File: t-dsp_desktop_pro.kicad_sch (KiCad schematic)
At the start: 177 parts, among them IC1 Logic Level Shifter - 74HCT2G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, J1 jumper, J10 JST-XH Connector -, J11 JST-XH Connector -, J12 RGB LED HEADEER, J13 Conn_01x02, J14 Conn_01x03, J15 Conn_01x01, J16 Conn_01x02, J17 Conn_02x04_Odd_Even, J18 Conn_02x02_Odd_Even, J2 GROUND HEADER, J3 jumper, J4 jumper, J5 jumper, J6 jumper, J7 jumper, J8 PJRAS2X1S01X, J9 PJRAS2X1S01X, SW1 SW_SPST, SW2 TL1105WF160Q - 3.15mm actuator, SW3 SW_SPST, SW4 SW_SPST, SW5 RotaryEncoder_Switch_MP, SW6 TL1105WF160Q - 3.15mm actuator, SW7 TL1105WF160Q - 3.15mm actuator, SW8 TL1105WF160Q - 3.15mm actuator, T108 Tab, T109 Tab, T110 Tab, T111 Tab, U1 Teensy 4.1 - DEVKIT, U2 ESP32-DevKitC - DEVKIT, U3 Power Mux & Protect - TPS2116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, U4 Optoisolators - H11L1SM - 6-S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, U5 Dual Buffer - SN74LVC2G125DCTR, U6 Dual Buffer - SN74LVC2G125DCTR, U7 Dual Buffer - SN74LVC2G125DCTR, U8 Dual Buffer - SN74LVC2G125DCTR, U9 Dual Buffer - 74HCT2G17GW,125

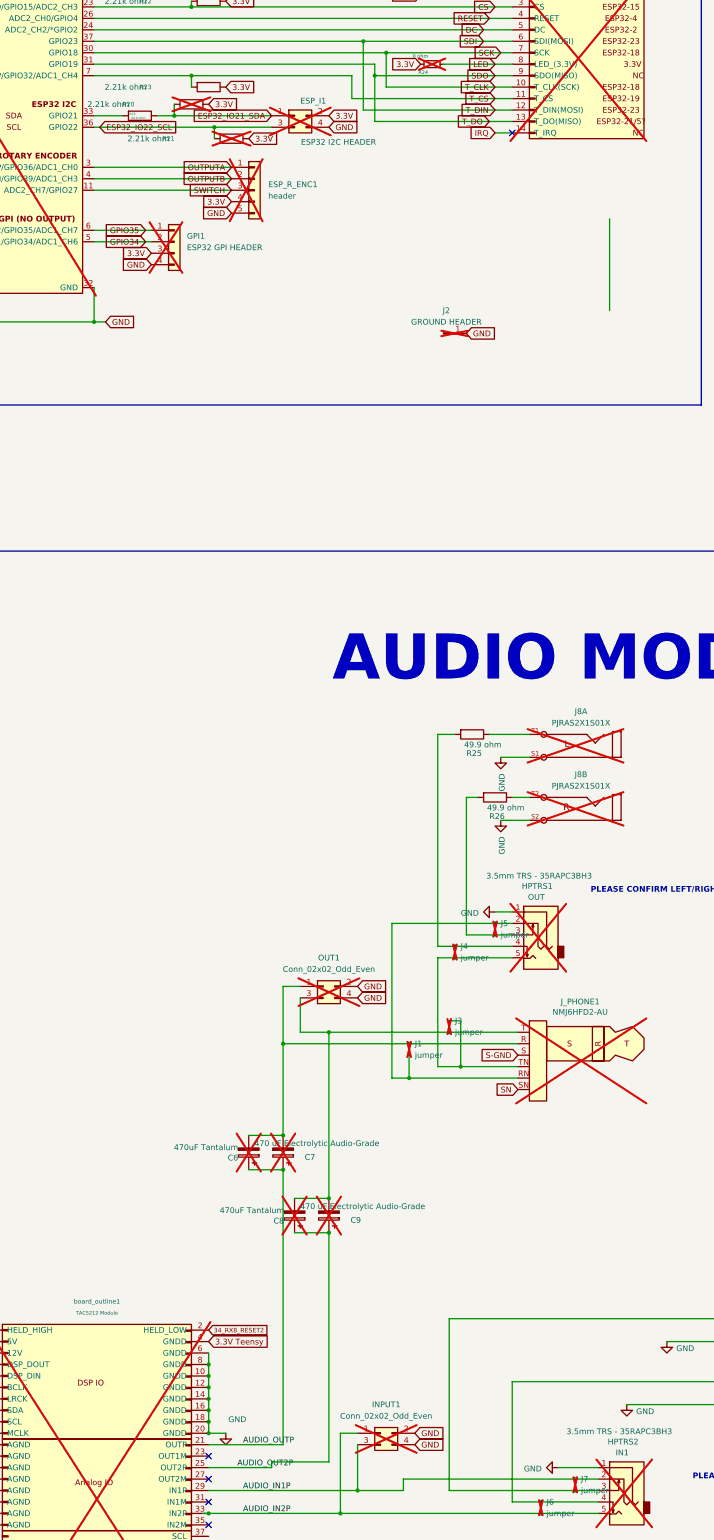
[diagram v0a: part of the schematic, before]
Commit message: Localize all 3D model paths for Docker/CI rendering
Rewrite all 3D model references from system variables (KICAD9_3DMODEL_DIR,
KISYS3DMOD, KICAD6/8_3DMODEL_DIR) to ${KIPRJMOD}/3d_models/ so models
resolve correctly in Docker-based KiBot CI builds. Copy 45 standard KiCad
3D models to the project. Fix BOM field mismatches for RLED1/RLED2 and
R36/R39 grouping. Update schematic symbol library and footprint libraries.

Co-Authored-By: Claude Opus 4.6 <noreply@anthropic.com>
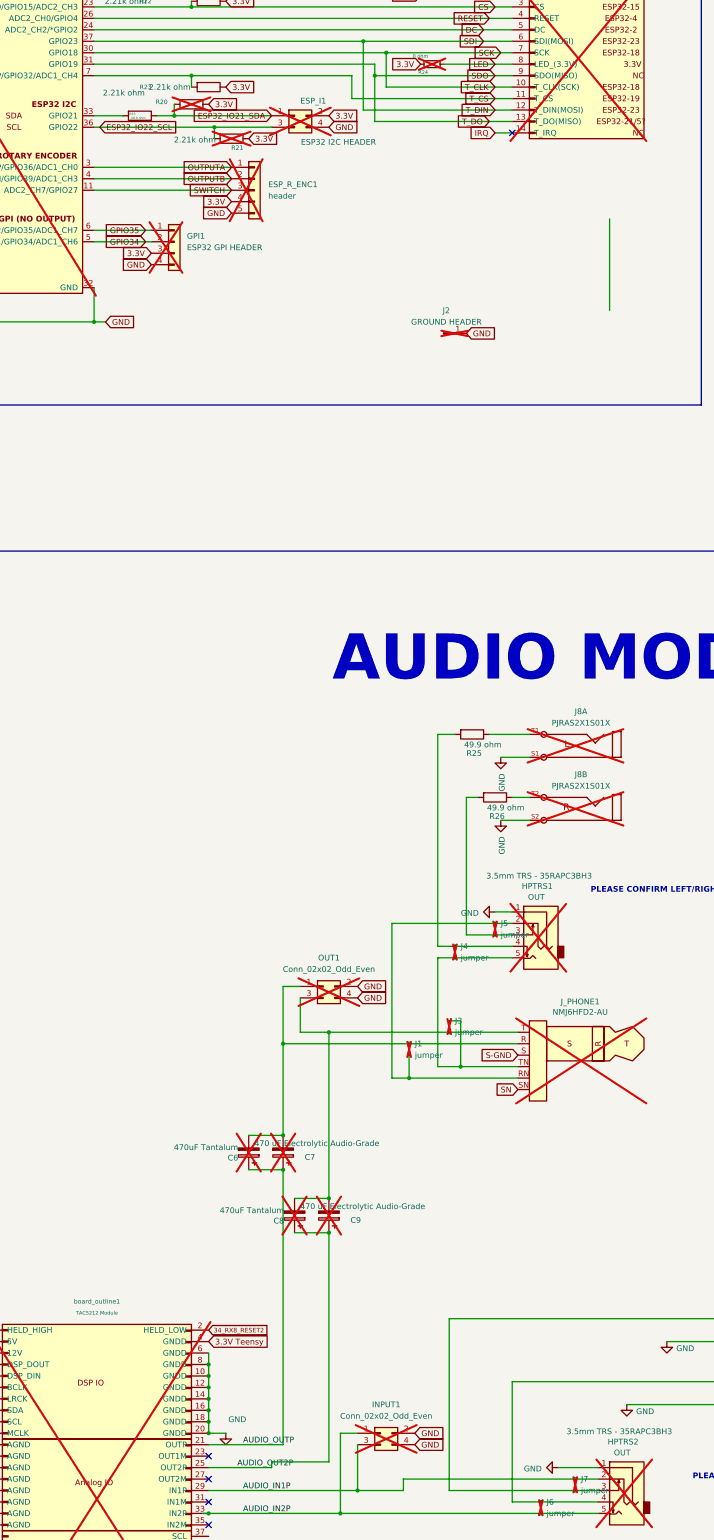
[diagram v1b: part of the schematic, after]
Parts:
- HPTRS1: symbol 35RAPC3BH3:AudioJack3_SwitchTR -> project_sch:HPTRS1
- HPTRS2: symbol 35RAPC3BH3:AudioJack3_SwitchTR -> project_sch:HPTRS1; Label IN1 -> OUT
- R20, R21: now in the parts list
- R36, R39: Manufacturer YAGEO -> Bourns; Manufacturer_Part_Number RC0805JR-0747RL -> CR0805-FX-2200ELF
- RLED1, RLED2: Digikey P100BYCT-ND -> ERJ-PA2F2211X-ND; Manufacturer Bourns -> YAGEO; Manufacturer_Part_Number CMP0805AFX-1000ELF -> RC0805DR-072K2L
- board_outline1: footprint project_fp:audio_module_board_outline_50x34.5_d1_mod -> project_fp:audio_module_board_outline_50x34.5_d1
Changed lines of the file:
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@@
 	)
 	(symbol
-		(lib_name "AudioJack3_SwitchTR_1")
-		(lib_id "35RAPC3BH3:AudioJack3_SwitchTR")
+		(lib_id "project_sch:HPTRS1")
 		(at 533.4 695.96 0)
 		(mirror y)
@@
 			)
 		)
-		(property "Label" "IN1"
+		(property "Label" "OUT"
 			(at 533.654 690.118 0)
 			(effects
@@
 		(unit 1)
 		(exclude_from_sim no)
-		(in_bom no)
+		(in_bom yes)
 		(on_board yes)
 		(dnp yes)
 		(property "Reference" "R21"
-			(at 433.07 398.78 90)
+			(at 448.31 400.812 90)
 			(effects
 				(font
@@
 		)
 		(property "Value" "2.21k ohm"
-			(at 428.625 398.78 90)
+			(at 438.912 399.034 90)
 			(effects
 				(font
@@
 		(unit 1)
 		(exclude_from_sim no)
-		(in_bom no)
+		(in_bom yes)
 		(on_board yes)
 		(dnp yes)
 		(property "Reference" "R20"
-			(at 424.18 391.16 90)
+			(at 431.546 390.652 90)
 			(effects
 				(font
@@
 		)
 		(property "Value" "2.21k ohm"
-			(at 419.735 391.16 90)
+			(at 433.324 387.35 90)
 			(effects
 				(font
@@
 			)
 		)
-		(property "Footprint" "project_fp:audio_module_board_outline_50x34.5_d1_mod"
+		(property "Footprint" "project_fp:audio_module_board_outline_50x34.5_d1"
 			(at 416.56 703.58 0)
 			(effects
@@
 			)
 		)
-		(property "Description" ""
+		(property "Description" "RES SMD 2.21 KOHM 1% 1/5W 0402"
 			(at 760.73 312.42 0)
 			(effects
@@
 					(size 1.27 1.27)
 				)
+				(hide yes)
 			)
 		)
-		(property "Manufacturer_Part_Number" "CMP0805AFX-1000ELF"
+		(property "Manufacturer_Part_Number" "RC0805DR-072K2L"
 			(at 760.73 312.42 0)
 			(effects
@@
 			)
 		)
-		(property "Digikey" "P100BYCT-ND"
+		(property "Digikey" "ERJ-PA2F2211X-ND"
 			(at 760.73 312.42 0)
 			(effects
@@
 			)
 		)
-		(property "Manufacturer" "Bourns"
+		(property "Manufacturer" "YAGEO"
 			(at 760.73 312.42 0)
 			(effects
@@
 			)
 		)
-		(property "Description" ""
+		(property "Description" "RES SMD 2.21 KOHM 1% 1/5W 0402"
 			(at 760.73 297.18 0)
 			(effects
@@
 					(size 1.27 1.27)
 				)
+				(hide yes)
 			)
 		)
-		(property "Manufacturer_Part_Number" "CMP0805AFX-1000ELF"
+		(property "Manufacturer_Part_Number" "RC0805DR-072K2L"
 			(at 760.73 297.18 0)
 			(effects
@@
 			)
 		)
-		(property "Digikey" "P100BYCT-ND"
+		(property "Digikey" "ERJ-PA2F2211X-ND"
 			(at 760.73 297.18 0)
 			(effects
@@
 			)
 		)
-		(property "Manufacturer" "Bourns"
+		(property "Manufacturer" "YAGEO"
 			(at 760.73 297.18 0)
 			(effects
@@
 		)
 		(property "Value" "2.21k ohm"
-			(at 423.545 387.35 90)
+			(at 423.164 388.62 90)
 			(effects
 				(font
@@
 			)
 		)
-		(property "Manufacturer" "YAGEO"
+		(property "Manufacturer" "Bourns"
 			(at 878.84 565.15 0)
 			(effects
@@
 			)
 		)
-		(property "Manufacturer_Part_Number" "RC0805JR-0747RL"
+		(property "Manufacturer_Part_Number" "CR0805-FX-2200ELF"
 			(at 878.84 565.15 0)
 			(effects
@@
 	)
 	(symbol
-		(lib_name "AudioJack3_SwitchTR_1")
-		(lib_id "35RAPC3BH3:AudioJack3_SwitchTR")
+		(lib_id "project_sch:HPTRS1")
 		(at 514.35 572.77 0)
 		(mirror y)
@@
 			)
 		)
-		(property "Manufacturer" "YAGEO"
+		(property "Manufacturer" "Bourns"
 			(at 872.49 586.74 0)
 			(effects
@@
 			)
 		)
-		(property "Manufacturer_Part_Number" "RC0805JR-0747RL"
+		(property "Manufacturer_Part_Number" "CR0805-FX-2200ELF"
 			(at 872.49 586.74 0)
 			(effects

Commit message: v0.8: Pre-production review - USB ESD, reverse polarity, boot pin fixes
- Add USB-C ESD protection: TPD4E02B04 (D+/D-/CC1/CC2) + TPD1E10B06 (VBUS)
- Add P-FET reverse polarity protection: DMG2307L-7 on 5V and 12V inputs
- Fix USB-C reversibility: tie DP1+DP2 and DN1+DN2 together
- Add ESP32 GPIO12 pull-down (10k) for 3.3V flash boot
- Add ESP32 GPIO17 CS pull-up (10k)
- Change SPI CS pull-ups R19/R22/R23 from 2.21k to 10k
- Add 12V LED power indicator (PWR3 + RLED3 6.8k)
- Change 5V LED resistors RLED1/RLED2 to 1k
- Add 3D models and footprints for new components
- Remove old gerbers directory (manufacturing outputs now via CI/CD)
- 8-layer PCB layout with full LCSC codes for JLCPCB assembly

Co-Authored-By: Claude Opus 4.6 <noreply@anthropic.com>
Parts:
- added C31, C33, C34: 10 uF, project_fp:C_0805_2012Metric_Pad1.15x1.40mm_HandSolder, symbol TEENSY_4.0_ESP32_AUDIO-rescue:C_Small-Device
- added C32, C35: 0.1 uF, project_fp:C_0805_2012Metric_Pad1.15x1.40mm_HandSolder, symbol TEENSY_4.0_ESP32_AUDIO-rescue:C_Small-Device
- added D5: TPD1E10B06DPYT, project_fp:TPD1E10B06DPYT, symbol TPD1E10B06DPYT:TPD1E10B06DPYT
- added ILI_LED2: jumper, project_fp:SolderJumper-3_P1.3mm_Bridged2Bar12_Pad1.0x1.5mm_NumberLabels, symbol Jumper:SolderJumper_3_Bridged12
- added J19: Conn_01x01, project_fp:OUT1B_PinHeader_1x01_P2.54mm_Vertical, symbol Connector_Generic:Conn_01x01
- added J20: Conn_01x01, project_fp:USB_5V_PinHeader_1x01_P2.54mm_Vertical, symbol Connector_Generic:Conn_01x01
- added PU_EN108: JUMPER, project_fp:SolderJumper-2_Open_Pad0.5x1.0mm_PU, symbol proejct_lib:NetTie_2
- added PWR3: LED Power Indicator - 1206 5v 2.0 V Forward, project_fp:LED_1210_3225Metric_Pad1.42x2.65mm_HandSolder, symbol Device:LED
- added Q1, Q2: DMG2307L-7, project_fp:DMG2307L-7, symbol DMG2307L-7:DMG2307L-7
- added RLED3: 6.8K, project_fp:R_0805_2012Metric_Pad1.15x1.40mm_HandSolder, symbol Device:R
- added U10: TPD4E02B04DQA, Package_SON:USON-10_2.5x1.0mm_P0.5mm, symbol project_sch:TPD4E02B04DQA-VERSION_B
- C1, C29, C30: LCSC C1848 -> C6119929; LCSC_MPN (none) -> CGA0805X7R105K500MT; LCSC_Manufacturer (none) -> HRE
- C12, C13, C23: LCSC_MPN (none) -> CL21A106KAYNNNE; LCSC_Manufacturer (none) -> Samsung Electro-Mechanics
- C14, C16, C17, C18, C19, C2, C20, C21, C22, C3, C4, C5: LCSC_MPN (none) -> CC0805KRX7R9BB104; LCSC_Manufacturer (none) -> YAGEO
- C15: LCSC_MPN (none) -> CL31A107MQHNNNE; LCSC_Manufacturer (none) -> Samsung Electro-Mechanics
- C27, C28: LCSC TYPE (none) -> SMD; LCSC_MPN (none) -> CL21A476MQYNNNE; LCSC_Manufacturer (none) -> Samsung Electro-Mechanics
- CC1, CC2, R29, R30: LCSC C2021 -> C27834; LCSC_MPN (none) -> 0805W8F5101T5E; LCSC_Manufacturer (none) -> UNI-ROYAL; Manufacturer_Part_Number ERJ-PB6D5101V -> 0805W8F5101T5E
- D2: LCSC_MPN (none) -> 1N4148W; LCSC_Manufacturer (none) -> ST(Semtech)
- D3, D4: LCSC_MPN (none) -> SK6812SIDE-A; LCSC_Manufacturer (none) -> OPSCO Optoelectronics
- HPTRS2: Label OUT -> IN
- IC1: LCSC_MPN (none) -> 74HCT2G125DC,125; LCSC_Manufacturer (none) -> Nexperia
- J13: footprint project_fp:PinHeader_1x02_P2.54mm_Vertical_NO_CTYD -> project_fp:T_SERIAL_PinHeader_1x02_P2.54mm_Vertical_NO_CTYD
- J16: footprint project_fp:PinHeader_1x02_P2.54mm_Vertical_NO_CTYD -> project_fp:T_BUTTON_PinHeader_1x02_P2.54mm_Vertical_NO_CTYD
- PWR1, PWR2: footprint Diode_SMD:D_1210_3225Metric_Pad1.42x2.65mm_HandSolder -> project_fp:LED_1210_3225Metric_Pad1.42x2.65mm_HandSolder; LCSC_MPN (none) -> NCD1206R1; LCSC_Manufacturer (none) -> NATIONSTAR
- R1, R2, R40, R41, R42, R43, R44, R45, R46, R47, R5, R6, R7, R9: Digikey P100BYCT-ND -> (none); LCSC_MPN (none) -> 0805W8F499JT5E; LCSC_Manufacturer (none) -> UNI-ROYAL; Manufacturer Bourns -> (none); Manufacturer_Part_Number CMP0805AFX-1000ELF -> (none)
- R10: footprint project_fp:R_0805_2012Metric_Pad1.20x1.40mm_HandSolder -> project_fp:R_0805_2012Metric_Pad1.15x1.40mm_HandSolder; Digikey P100BYCT-ND -> (none); LCSC_MPN (none) -> 0805W8F499JT5E; LCSC_Manufacturer (none) -> UNI-ROYAL; Manufacturer Bourns -> (none); Manufacturer_Part_Number CMP0805AFX-1000ELF -> (none); now fitted
- R11, R13, R14, R16, R17: LCSC_MPN (none) -> 0805W8F2201T5E; LCSC_Manufacturer (none) -> UNI-ROYAL
- R12, R15, R27, R31, R35, R48, R49, R50, R51: LCSC_MPN (none) -> 0805W8F0000T5E; LCSC_Manufacturer (none) -> UNI-ROYAL
- R18, R32, R34, R36, R37, R38, R39, R8: LCSC_MPN (none) -> 0805W8F2200T5E; LCSC_Manufacturer (none) -> UNI-ROYAL
- R19, R22, R23: value 2.21k ohm -> 10k; Digikey ERJ-PA2F2211X-ND -> (none); LCSC C17520 -> C17414; LCSC_MPN (none) -> 0805W8F1002T5E; LCSC_Manufacturer (none) -> UNI-ROYAL; Manufacturer YAGEO -> (none); Manufacturer_Part_Number RC0805DR-072K2L -> (none)
- R20, R21: LCSC_MPN (none) -> 0805W8F2201T5E; LCSC_Manufacturer (none) -> UNI-ROYAL; now fitted
- R24: value 0 ohm -> 49.9 ohm; LCSC (none) -> C17720; LCSC TYPE (none) -> SMD; LCSC_MPN (none) -> 0805W8F499JT5E; LCSC_Manufacturer (none) -> UNI-ROYAL; now fitted; now in the parts list
- R25, R26, R3, R4, R52: LCSC_MPN (none) -> 0805W8F499JT5E; LCSC_Manufacturer (none) -> UNI-ROYAL
- R28: LCSC_MPN (none) -> 0805W8F1692T5E; LCSC_Manufacturer (none) -> UNI-ROYAL
- R33: LCSC_MPN (none) -> 0805W8F1501T5E; LCSC_Manufacturer (none) -> UNI-ROYAL
- R53: value 49.9 ohm -> 10k; LCSC C17720 -> C17414; LCSC_MPN (none) -> 0805W8F1002T5E; LCSC_Manufacturer (none) -> UNI-ROYAL
- RLED1, RLED2: value 2.21k ohm -> 1k; Digikey ERJ-PA2F2211X-ND -> (none); LCSC C17520 -> C17513; LCSC_MPN (none) -> 0805W8F1001T5E; LCSC_Manufacturer (none) -> UNI-ROYAL; Manufacturer YAGEO -> (none); Manufacturer_Part_Number RC0805DR-072K2L -> (none)
- U1: symbol teensy:Teensy4.1 -> project_sch:Teensy4.1_no_ethernet; now in the parts list
- U2: symbol project_lil_2:ESP32-DevKitC_modified -> project_sch:ESP32-DevKitC_modified; now in the parts list
- U3: footprint Package_TO_SOT_SMD:SOT-583-8 -> project_fp:TPS2116DRL; LCSC_MPN (none) -> TPS2116DRLR; LCSC_Manufacturer (none) -> TI
- U4: LCSC_MPN (none) -> H11L1SM; LCSC_Manufacturer (none) -> onsemi
- U5, U6, U7, U8: LCSC_MPN (none) -> SN74LVC2G125DCTR; LCSC_Manufacturer (none) -> TI
- U9: LCSC_MPN (none) -> 74HCT2G17GW,125; LCSC_Manufacturer (none) -> Nexperia
- USBC1: LCSC_MPN (none) -> USB4085-GF-A; LCSC_Manufacturer (none) -> Global Connector Technology
- board_outline1: symbol global_lib:TAC5212_breakout -> project_sch:TAC5212_breakout; now in the parts list
- renumbered ILI_VCC1 to ILI_LED1
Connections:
- net 12V: now also Q2.3 (D), RLED3.2; no longer J11.1 (Pin_1)
- net 3.3V: now also PU_EN108.1; no longer ILI_LED1.3 (B), R20.1, R21.1
- net 5V: now also ILI1.1 (VCC_(5V)), board_outline2.15 (VCC), C34.1, C35.1; no longer ILI_LED1.1 (A)
- net 5V_JST: now also Q1.3 (D); no longer J10.1 (Pin_1)
- net 5V_USB: now also D5.1
- net DEVICE_D1+: now also U10.9 (NC); no longer USBC1.A6 (DP1)
- net DEVICE_D1-: now also U10.7 (NC); no longer USBC1.A7 (DN1)
- net ESP32_IO12_SPI_MISO: now also R53.1
- net ESP32_IO21_SDA: now also U2.33 (GPIO21), ILI_LED2.3 (B); no longer R53.1
- net ESP32_IO22_SCL: now also ILI_LED1.3 (B)
- net GND: now also R53.2, U3.1 (GND), U8.1 (~{1OE}), U8.7 (~{2OE}), board_outline1.39 (GNDD), board_outline1.49 (AGND), board_outline1.50 (AGND), C31.2, C32.2, C33.2, C34.2, C35.2, D5.2, PWR3.1 (K), Q1.1 (G), Q2.1 (G), U10.3 (G), U10.8 (G); no longer U1.64 (GND), board_outline1.47 (GNDD)
- net HOST_5V: now also C33.1
- net IRQ: now also ILI_LED2.2 (C)
- net LED: now also ILI_LED1.2 (C); no longer R24.2, U1.61 (LED)
- net MCLK2: now also J19.1 (Pin_1)
- net VIN2_SECONDARY: now also J20.1 (Pin_1)
- net at CC1.2: now also U10.10 (NC); no longer USBC1.A5 (CC1)
- net at USBC1.B5 (CC2): now also U10.5 (IO4); no longer CC2.2
- net at USBC1.B6 (DP2): now also USBC1.A6 (DP1), U10.2 (IO2)
- net at USBC1.B7 (DN2): now also USBC1.A7 (DN1), U10.4 (IO3)
- removed net RX+: U1.60 (R+)
- removed net RX-: U1.65 (R-)
- removed net TX+: U1.63 (T+)
- removed net TX-: U1.62 (T-)
- removed net VCC: ILI1.1 (VCC_(5V)), ILI_LED1.2 (C), board_outline2.15 (VCC)
- new net: C31.1, C32.1, J11.1 (Pin_1), Q2.2 (S)
- new net: J10.1 (Pin_1), Q1.2 (S)
- new net: PU_EN108.2, R20.1, R21.1
- new net: U10.1 (IO1), USBC1.A5 (CC1)
- new net: CC2.2, U10.6 (NC)
- new net: PWR3.2 (A), RLED3.1
- new net: ILI_LED1.1 (A), R24.2
- no-connect marks 14 -> 19
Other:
- note added: "5V PRIORITY SWITCHOVER + INRUSH LIMITING"
- note removed: "POWER LED"
- moved on the sheet: C1, C10, C11, C12, C13, C14, C15, C16, C17, C18, C19, C20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
